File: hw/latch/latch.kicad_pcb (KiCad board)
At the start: 2 copper layers, 80 x 45 mm, 19 parts, among them J1 HDR_2.54_1x05

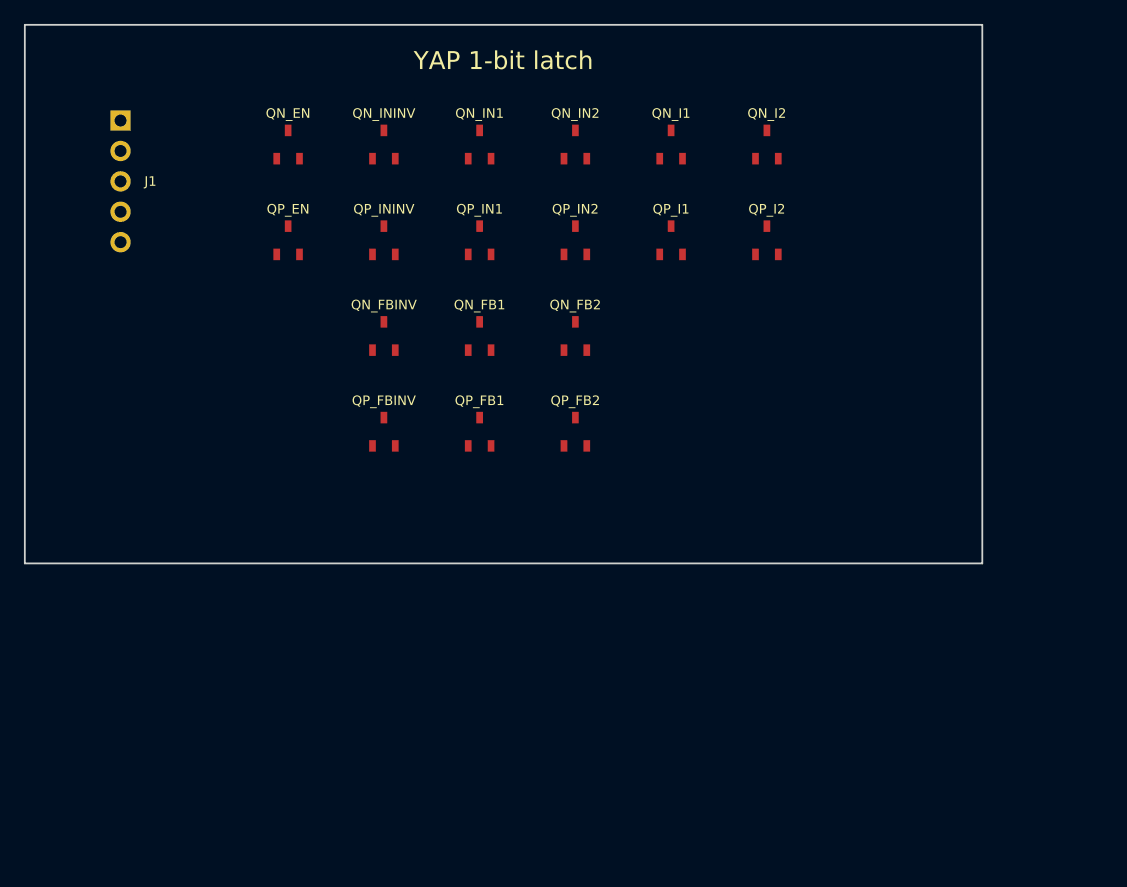
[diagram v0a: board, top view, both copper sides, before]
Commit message: Route physical-cpu m12 latch PCB and add assembly table
Pads that share a net are tied by copper. assembly.md is the MOSFET pin map.
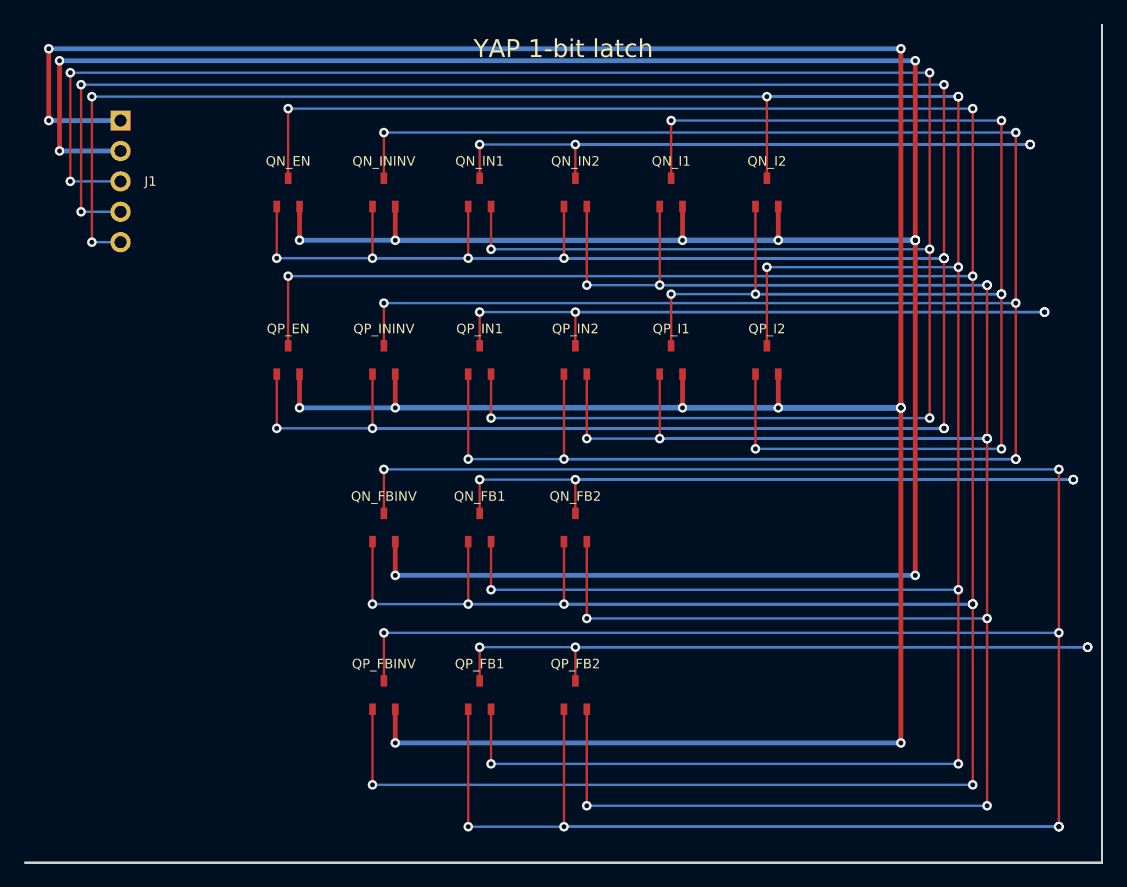
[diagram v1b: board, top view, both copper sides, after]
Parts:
- moved QP_FB1 22.0 mm to (38.0, 56.0)
- moved QP_FB2 22.0 mm to (46.0, 56.0)
- moved QP_FBINV 22.0 mm to (30.0, 56.0)
- moved QN_FB1 16.0 mm to (38.0, 42.0)
- moved QN_FB2 16.0 mm to (46.0, 42.0)
- moved QN_FBINV 16.0 mm to (30.0, 42.0)
- moved QP_EN 10.0 mm to (22.0, 28.0)
- moved QP_I1 10.0 mm to (54.0, 28.0)
- moved QP_I2 10.0 mm to (62.0, 28.0)
- moved QP_IN1 10.0 mm to (38.0, 28.0)
- moved QP_IN2 10.0 mm to (46.0, 28.0)
- moved QP_ININV 10.0 mm to (30.0, 28.0)
- moved QN_EN 4.00 mm to (22.0, 14.0)
- moved QN_I1 4.00 mm to (54.0, 14.0)
- moved QN_I2 4.00 mm to (62.0, 14.0)
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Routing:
- net EN: track 0.00 -> 419.6 mm, vias 0 -> 15
- net ENB: track 0.00 -> 381.1 mm, vias 0 -> 12
- net VDD: track 0.00 -> 318.5 mm, vias 0 -> 13
- net VSS: track 0.00 -> 310.5 mm, vias 0 -> 13
- net Q: track 0.00 -> 274.8 mm, vias 0 -> 11
- net N1: track 0.00 -> 270.4 mm, vias 0 -> 12
- net ENB_FB: track 0.00 -> 260.7 mm, vias 0 -> 8
- net ENB_IN: track 0.00 -> 238.0 mm, vias 0 -> 8
- net D: track 0.00 -> 194.5 mm, vias 0 -> 7
- net QB: track 0.00 -> 146.4 mm, vias 0 -> 8
- net MIDP_FB: track 0.00 -> 99.2 mm, vias 0 -> 4
- net MIDN_FB: track 0.00 -> 96.8 mm, vias 0 -> 4
- net MIDP_IN: track 0.00 -> 92.0 mm, vias 0 -> 4
- net MIDN_IN: track 0.00 -> 89.6 mm, vias 0 -> 4
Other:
- board size 80 x 45 mm -> 90 x 70 mm
